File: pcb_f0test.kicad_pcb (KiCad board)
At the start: 2 copper layers, 50 x 50 mm, 88 parts, among them P1 CONN_02X05, P2 CONN_01X02, P3 CONN_01X06, P5 CONN_02X05, P6 CONN_02X05, P7 CONN_01X01, P8 CONN_01X01, U1 STM32F042GxU, U2 LP2985LV, U3 KNUSB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

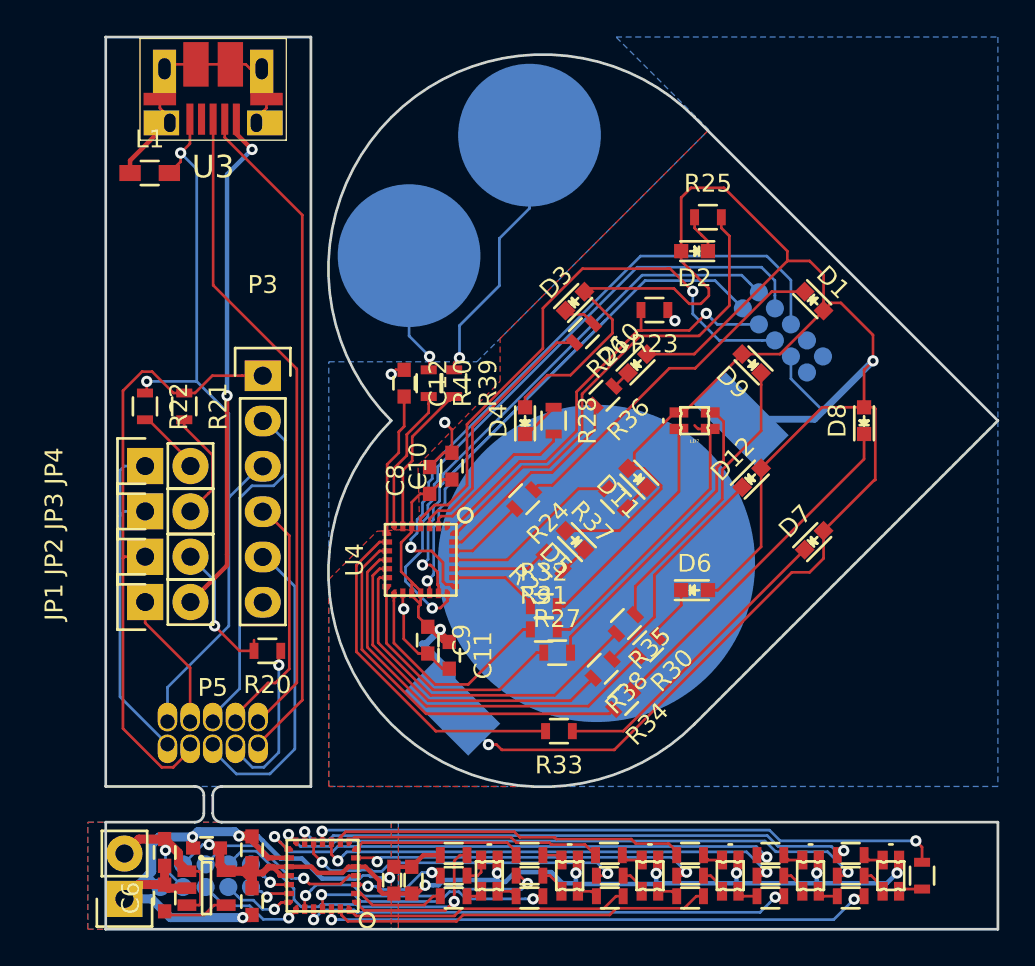
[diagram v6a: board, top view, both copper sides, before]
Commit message: Fix PCB outline (might still need a bit of tweaks for the ring).
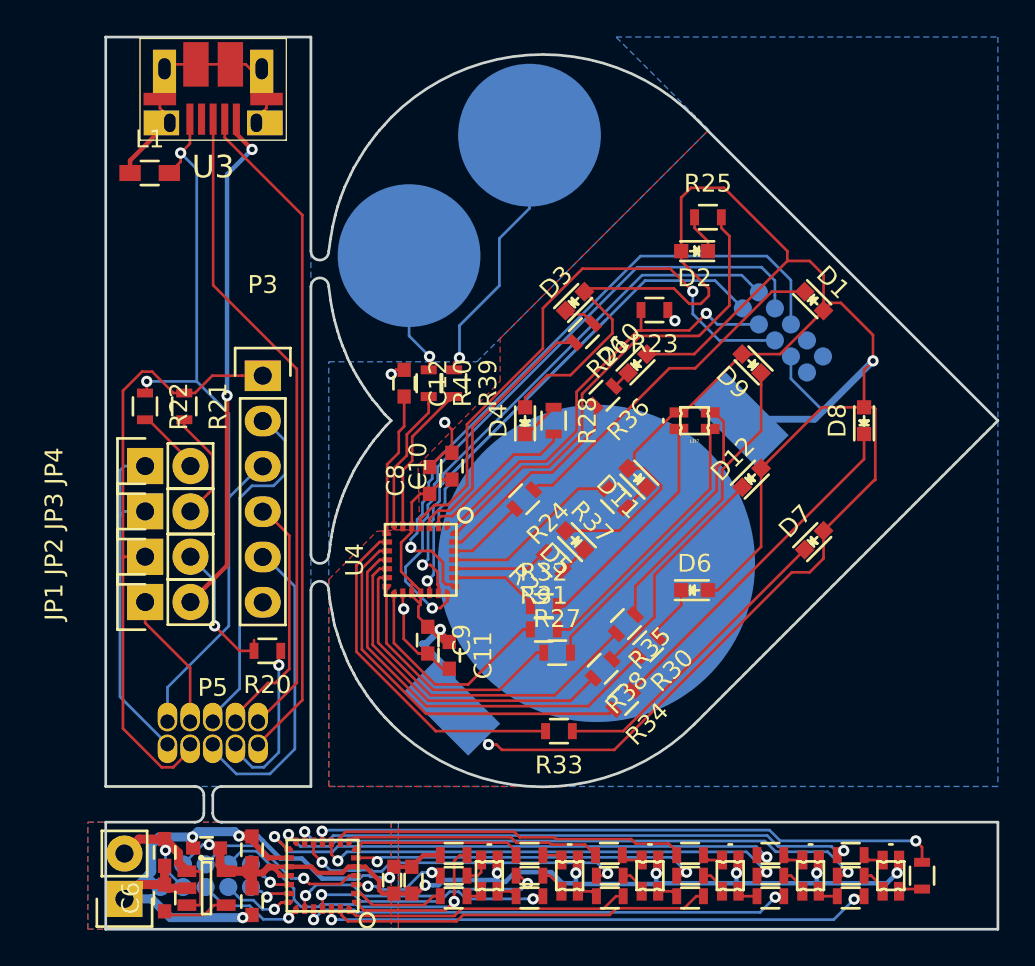
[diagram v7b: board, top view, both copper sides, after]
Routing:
- net /sheet_heart/h_ildg1: track 16.2 -> 15.2 mm
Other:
- outline, holes or cut-outs redrawn
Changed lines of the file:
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@@
     (links 207)
     (no_connects 1)
-    (area 23.064267 12.98448 77.075001 70.4649)
+    (area 26.924999 15.924999 77.075001 66.075001)
     (thickness 0.8)
-    (drawings 33)
-    (tracks 988)
+    (drawings 117)
+    (tracks 986)
     (zones 0)
     (modules 88)
@@
     )
   )
+  (gr_line (start 38.5 47) (end 38.5 58) (layer Edge.Cuts) (width 0.15))
+  (gr_line (start 38.5 30) (end 38.5 45) (layer Edge.Cuts) (width 0.15))
+  (gr_arc (start 51.5 46) (end 60 54.5) (angle 90) (layer Edge.Cuts) (width 0.15))
+  (gr_line (start 42.99 54.48) (end 43 54.5) (layer Edge.Cuts) (width 0.15))
+  (gr_line (start 42.65 54.13) (end 42.99 54.48) (layer Edge.Cuts) (width 0.15))
+  (gr_line (start 42.38 53.83) (end 42.65 54.13) (layer Edge.Cuts) (width 0.15))
+  (gr_line (start 42.2 53.61) (end 42.38 53.83) (layer Edge.Cuts) (width 0.15))
+  (gr_line (start 41.88 53.21) (end 42.2 53.61) (layer Edge.Cuts) (width 0.15))
+  (gr_line (start 41.65 52.9) (end 41.88 53.21) (layer Edge.Cuts) (width 0.15))
+  (gr_line (start 41.51 52.68) (end 41.65 52.9) (layer Edge.Cuts) (width 0.15))
+  (gr_line (start 41.25 52.29) (end 41.51 52.68) (layer Edge.Cuts) (width 0.15))
+  (gr_line (start 41.04 51.95) (end 41.25 52.29) (layer Edge.Cuts) (width 0.15))
+  (gr_line (start 40.91 51.69) (end 41.04 51.95) (layer Edge.Cuts) (width 0.15))
+  (gr_line (start 40.7 51.3) (end 40.91 51.69) (layer Edge.Cuts) (width 0.15))
+  (gr_line (start 40.53 50.95) (end 40.7 51.3) (layer Edge.Cuts) (width 0.15))
+  (gr_line (start 40.4 50.6) (end 40.53 50.95) (layer Edge.Cuts) (width 0.15))
+  (gr_line (start 40.22 50.18) (end 40.4 50.6) (layer Edge.Cuts) (width 0.15))
+  (gr_line (start 40.1 49.84) (end 40.22 50.18) (layer Edge.Cuts) (width 0.15))
+  (gr_line (start 40 49.5) (end 40.1 49.84) (layer Edge.Cuts) (width 0.15))
+  (gr_line (start 39.83 48.98) (end 40 49.5) (layer Edge.Cuts) (width 0.15))
+  (gr_line (start 39.76 48.65) (end 39.83 48.98) (layer Edge.Cuts) (width 0.15))
+  (gr_line (start 39.7 48.31) (end 39.76 48.65) (layer Edge.Cuts) (width 0.15))
+  (gr_line (start 39.61 47.83) (end 39.7 48.31) (layer Edge.Cuts) (width 0.15))
+  (gr_line (start 39.54 47.42) (end 39.61 47.83) (layer Edge.Cuts) (width 0.15))
+  (gr_line (start 39.5 47) (end 39.54 47.42) (layer Edge.Cuts) (width 0.15))
+  (gr_arc (start 39 47) (end 38.5 47) (angle 180) (layer Edge.Cuts) (width 0.15))
+  (gr_arc (start 39 45) (end 39.5 45) (angle 180) (layer Edge.Cuts) (width 0.15))
+  (gr_line (start 39.54 44.81) (end 39.5 45) (layer Edge.Cuts) (width 0.15))
+  (gr_line (start 39.58 44.45) (end 39.54 44.81) (layer Edge.Cuts) (width 0.15))
+  (gr_line (start 39.64 44.02) (end 39.58 44.45) (layer Edge.Cuts) (width 0.15))
+  (gr_line (start 39.71 43.66) (end 39.64 44.02) (layer Edge.Cuts) (width 0.15))
+  (gr_line (start 39.8 43.21) (end 39.71 43.66) (layer Edge.Cuts) (width 0.15))
+  (gr_line (start 39.9 42.84) (end 39.8 43.21) (layer Edge.Cuts) (width 0.15))
+  (gr_line (start 40 42.5) (end 39.9 42.84) (layer Edge.Cuts) (width 0.15))
+  (gr_line (start 40.15 42.04) (end 40 42.5) (layer Edge.Cuts) (width 0.15))
+  (gr_line (start 40.26 41.73) (end 40.15 42.04) (layer Edge.Cuts) (width 0.15))
+  (gr_line (start 40.4 41.39) (end 40.26 41.73) (layer Edge.Cuts) (width 0.15))
+  (gr_line (start 40.6 40.94) (end 40.4 41.39) (layer Edge.Cuts) (width 0.15))
+  (gr_line (start 40.75 40.62) (end 40.6 40.94) (layer Edge.Cuts) (width 0.15))
+  (gr_line (start 40.91 40.3) (end 40.75 40.62) (layer Edge.Cuts) (width 0.15))
+  (gr_line (start 41.16 39.87) (end 40.91 40.3) (layer Edge.Cuts) (width 0.15))
+  (gr_line (start 41.3 39.64) (end 41.16 39.87) (layer Edge.Cuts) (width 0.15))
+  (gr_line (start 41.55 39.26) (end 41.3 39.64) (layer Edge.Cuts) (width 0.15))
+  (gr_line (start 41.8 38.91) (end 41.55 39.26) (layer Edge.Cuts) (width 0.15))
+  (gr_line (start 42.02 38.6) (end 41.8 38.91) (layer Edge.Cuts) (width 0.15))
+  (gr_line (start 42.26 38.32) (end 42.02 38.6) (layer Edge.Cuts) (width 0.15))
+  (gr_line (start 42.52 38.01) (end 42.26 38.32) (layer Edge.Cuts) (width 0.15))
+  (gr_line (start 42.71 37.79) (end 42.52 38.01) (layer Edge.Cuts) (width 0.15))
+  (gr_line (start 43 37.5) (end 42.71 37.79) (layer Edge.Cuts) (width 0.15))
+  (gr_line (start 38.5 16) (end 38.5 28) (layer Edge.Cuts) (width 0.15))
+  (gr_arc (start 51.5 29) (end 43 20.5) (angle 90) (layer Edge.Cuts) (width 0.15))
+  (gr_line (start 42.65 37.16) (end 43 37.5) (layer Edge.Cuts) (width 0.15))
+  (gr_line (start 42.44 36.91) (end 42.65 37.16) (layer Edge.Cuts) (width 0.15))
+  (gr_line (start 42.2 36.6) (end 42.44 36.91) (layer Edge.Cuts) (width 0.15))
+  (gr_line (start 41.96 36.33) (end 42.2 36.6) (layer Edge.Cuts) (width 0.15))
+  (gr_line (start 41.78 36.08) (end 41.96 36.33) (layer Edge.Cuts) (width 0.15))
+  (gr_line (start 41.51 35.69) (end 41.78 36.08) (layer Edge.Cuts) (width 0.15))
+  (gr_line (start 41.28 35.33) (end 41.51 35.69) (layer Edge.Cuts) (width 0.15))
+  (gr_line (start 41.08 35) (end 41.28 35.33) (layer Edge.Cuts) (width 0.15))
+  (gr_line (start 40.9 34.68) (end 41.08 35) (layer Edge.Cuts) (width 0.15))
+  (gr_line (start 40.71 34.32) (end 40.9 34.68) (layer Edge.Cuts) (width 0.15))
+  (gr_line (start 40.55 33.99) (end 40.71 34.32) (layer Edge.Cuts) (width 0.15))
+  (gr_line (start 40.4 33.6) (end 40.55 33.99) (layer Edge.Cuts) (width 0.15))
+  (gr_line (start 40.26 33.28) (end 40.4 33.6) (layer Edge.Cuts) (width 0.15))
+  (gr_line (start 40.12 32.89) (end 40.26 33.28) (layer Edge.Cuts) (width 0.15))
+  (gr_line (start 40 32.5) (end 40.12 32.89) (layer Edge.Cuts) (width 0.15))
+  (gr_line (start 39.82 31.86) (end 40 32.5) (layer Edge.Cuts) (width 0.15))
+  (gr_line (start 39.7 31.32) (end 39.82 31.86) (layer Edge.Cuts) (width 0.15))
+  (gr_line (start 39.6 30.75) (end 39.7 31.32) (layer Edge.Cuts) (width 0.15))
+  (gr_line (start 39.5 30) (end 39.6 30.75) (layer Edge.Cuts) (width 0.15))
+  (gr_line (start 39.6 27.3) (end 39.5 28) (layer Edge.Cuts) (width 0.15))
+  (gr_line (start 39.72 26.62) (end 39.6 27.3) (layer Edge.Cuts) (width 0.15))
+  (gr_line (start 39.86 26) (end 39.72 26.62) (layer Edge.Cuts) (width 0.15))
+  (gr_line (start 40 25.49) (end 39.86 26) (layer Edge.Cuts) (width 0.15))
+  (gr_line (start 40.17 24.99) (end 40 25.49) (layer Edge.Cuts) (width 0.15))
+  (gr_line (start 40.4 24.39) (end 40.17 24.99) (layer Edge.Cuts) (width 0.15))
+  (gr_line (start 40.73 23.69) (end 40.4 24.39) (layer Edge.Cuts) (width 0.15))
+  (gr_line (start 40.91 23.32) (end 40.73 23.69) (layer Edge.Cuts) (width 0.15))
+  (gr_line (start 41.24 22.77) (end 40.91 23.32) (layer Edge.Cuts) (width 0.15))
+  (gr_line (start 41.54 22.28) (end 41.24 22.77) (layer Edge.Cuts) (width 0.15))
+  (gr_line (start 41.77 21.97) (end 41.54 22.28) (layer Edge.Cuts) (width 0.15))
+  (gr_line (start 42.17 21.43) (end 41.77 21.97) (layer Edge.Cuts) (width 0.15))
+  (gr_line (start 42.33 21.24) (end 42.17 21.43) (layer Edge.Cuts) (width 0.15))
+  (gr_line (start 42.61 20.93) (end 42.33 21.24) (layer Edge.Cuts) (width 0.15))
+  (gr_line (start 43 20.5) (end 42.61 20.93) (layer Edge.Cuts) (width 0.15))
+  (gr_arc (start 39 30) (end 38.5 30) (angle 180) (layer Edge.Cuts) (width 0.15))
+  (gr_arc (start 39 28) (end 39.5 28) (angle 180) (layer Edge.Cuts) (width 0.15))
   (gr_circle (center 60 37.5) (end 64.5 37.5) (layer Dwgs.User) (width 0.2))
   (gr_circle (center 60 37.5) (end 67 37.5) (layer Dwgs.User) (width 0.2))
@@
   (gr_circle (center 50.75 21.5) (end 54.75 21.5) (layer B.SilkS) (width 0.2))
   (gr_line (start 77 37.5) (end 60 20.5) (layer Edge.Cuts) (width 0.15))
-  (gr_arc (start 51.5 29) (end 43 37.5) (angle 180) (layer Edge.Cuts) (width 0.15))
-  (gr_arc (start 51.5 46) (end 60 54.5) (angle 180) (layer Edge.Cuts) (width 0.15))
   (gr_line (start 60 54.5) (end 77 37.5) (layer Edge.Cuts) (width 0.15))
   (gr_line (start 33.5 60) (end 77 60) (layer Edge.Cuts) (width 0.15))
@@
   (gr_arc (start 32 59.5) (end 32.5 59.5) (angle 90) (layer Edge.Cuts) (width 0.15))
   (gr_line (start 27 60) (end 32 60) (layer Edge.Cuts) (width 0.15))
-  (gr_line (start 38.5 16) (end 38.5 58) (layer Edge.Cuts) (width 0.15))
   (gr_line (start 27 16) (end 38.5 16) (layer Edge.Cuts) (width 0.15))
   (gr_line (start 27 58) (end 27 16) (layer Edge.Cuts) (width 0.15))
@@
   (segment (start 60.875 41.325) (end 53 49.2) (width 0.1524) (layer F.Cu) (net 80))
   (segment (start 53 49.2) (end 52.3 49.2) (width 0.1524) (layer F.Cu) (net 80))
-  (segment (start 60.875 37.9625) (end 60.1976 37.9625) (width 0.1524) (layer F.Cu) (net 80))
-  (segment (start 60.1976 37.9625) (end 60 37.7649) (width 0.1524) (layer F.Cu) (net 80))
   (segment (start 44.1 44.6) (end 44.1 44.15) (width 0.1524) (layer B.Cu) (net 82))
   (segment (start 44.1 44.15) (end 44.45 43.8) (width 0.1524) (layer B.Cu) (net 82))
@@
     (connect_pads (clearance 0.254))
     (min_thickness 0.2032)
-    (fill yes (arc_segments 16) (thermal_gap 0.2032) (thermal_bridge_width 0.254))
+    (fill yes (arc_segments 16) (thermal_gap 0.254) (thermal_bridge_width 0.3048))
     (polygon
       (pts

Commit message: Improved routing of the heart.
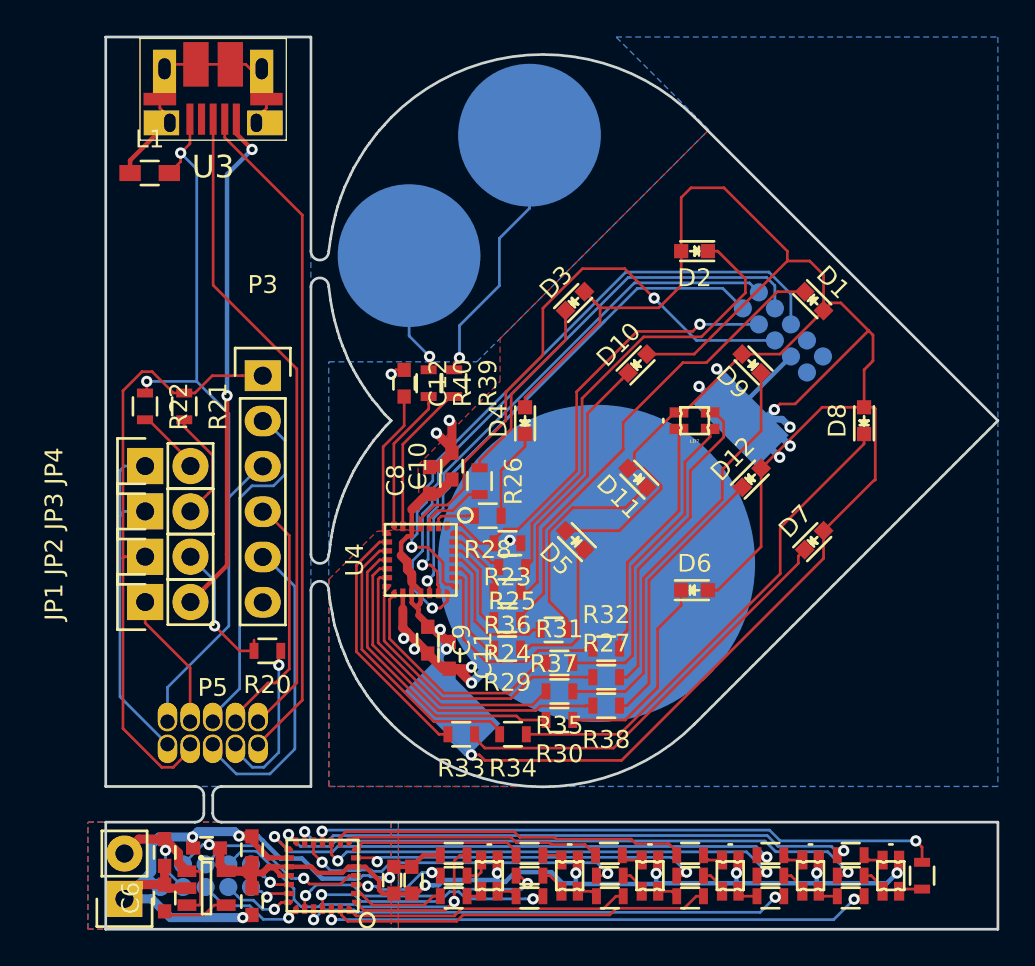
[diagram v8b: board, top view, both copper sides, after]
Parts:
- moved R25 22.5 mm to (49.8, 45.7), turned to 180 degrees
- moved R23 15.5 mm to (49.5, 44.4)
- moved R36 12.2 mm to (49.5, 47.1), turned to 180 degrees
- moved R26 10.1 mm to (48.0, 40.9), turned to 270 degrees
- moved R37 8.16 mm to (52.1, 49.2), turned to 180 degrees
- moved R24 6.84 mm to (49.5, 48.7), turned to 180 degrees
- moved R28 6.48 mm to (48.4, 42.8), turned to 180 degrees
- moved R34 6.47 mm to (49.8, 55.1), turned to 180 degrees
- moved R30 6.46 mm to (52.4, 54.3), turned to 180 degrees
- moved R29 5.53 mm to (49.5, 50.3), turned to 180 degrees
- moved R33 5.48 mm to (46.9, 55.1)
- moved R35 5.30 mm to (52.4, 52.7), turned to 180 degrees
- moved R32 4.23 mm to (55.0, 50.3)
- moved R27 3.07 mm to (55.0, 51.9)
- moved R38 2.08 mm to (55.0, 53.5), turned to 180 degrees
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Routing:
- net /sheet_heart/h_ld5: track 27.0 -> 3.20 mm
- net /sheet_heart/h_ild5: track 2.21 -> 25.9 mm
- net GNDD: track 10.9 -> 32.7 mm, vias 4 -> 8
- net +3V3: track 219.1 -> 235.6 mm, vias 11 -> 17
- net /sheet_heart/h_ild4: track 1.10 -> 15.0 mm
- net /sheet_heart/h_ld9: track 14.6 -> 3.79 mm
- net /sheet_heart/h_ild8: track 1.68 -> 12.4 mm
- net /sheet_heart/h_ild9: track 1.99 -> 10.8 mm
- net /sheet_heart/h_ild10: track 3.17 -> 11.5 mm
- net /sheet_heart/h_ild7: track 19.7 -> 27.7 mm
- net /sheet_heart/h_ld4: track 11.9 -> 3.95 mm
- net /sheet_heart/h_ild11: track 16.5 -> 23.9 mm
- net /sheet_heart/h_ldb1: track 5.05 -> 12.0 mm
- net /sheet_heart/h_ild6: track 1.70 -> 8.59 mm
- net /sheet_heart/h_ild1: track 19.8 -> 26.7 mm
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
